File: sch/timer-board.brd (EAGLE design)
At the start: 76.2 x 69.9 mm, 35 parts, among them IC1 ATMEGA328P

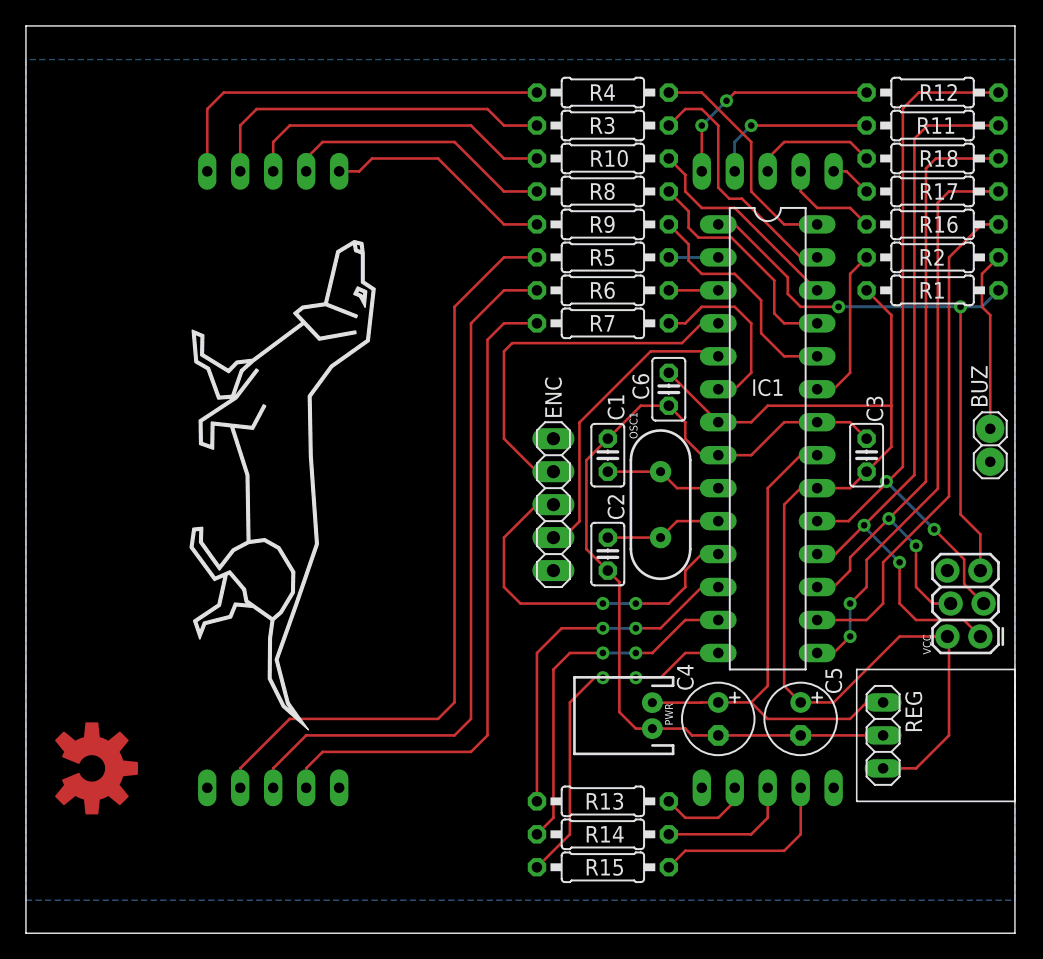
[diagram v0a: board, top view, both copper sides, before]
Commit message: feat: pcb added holes
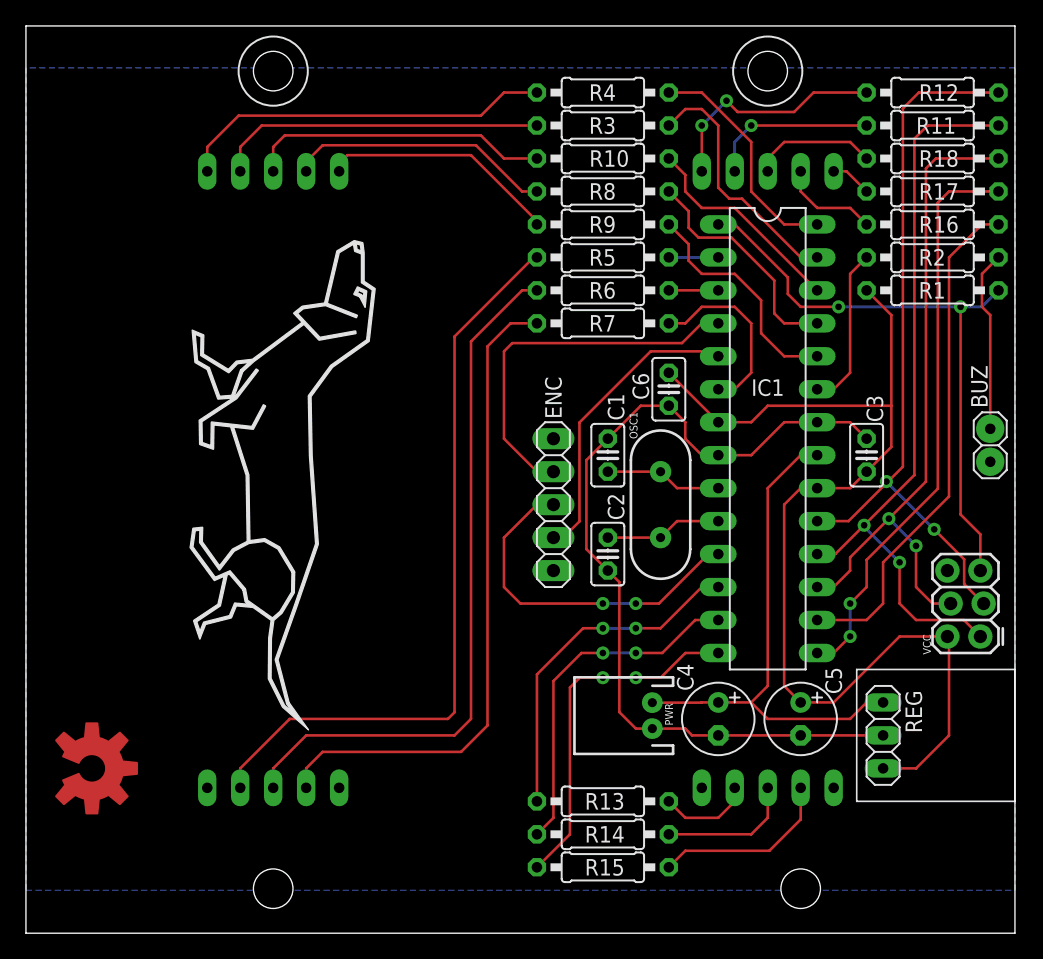
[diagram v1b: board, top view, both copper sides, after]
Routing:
- net N$1: track 27.4 -> 25.4 mm
- net N$2: track 30.7 -> 29.0 mm
- net D0C: track 27.5 -> 26.5 mm
- net N$3: track 58.5 -> 57.6 mm
- net N$9: track 24.2 -> 23.3 mm
- net N$4: track 54.9 -> 54.1 mm
- net BTN: track 28.0 -> 27.3 mm
- net N$5: track 51.3 -> 50.6 mm
- net N$7: track 17.8 -> 18.5 mm
- net N$14: track 17.3 -> 18.0 mm
- net D0E: track 26.8 -> 27.4 mm
- net N$17: track 14.8 -> 14.1 mm
- net D0D: track 27.5 -> 27.0 mm

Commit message: refactoring: reworked routing
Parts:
- removed C5: 100uF, rcl:E2,5-6
- removed REG: VREG_STEP_UP, parts:VREG
- added R19: (no value), rcl:0207/10
- added T1: 2N3904, transistor:TO92
- BUZ: value CONN_1X2 -> BUZZER2_IN_1; device parts:CONN_1X2 -> parts:BUZZER_2_IN_1
- C4: value 100uF -> 10uF
- LOGO1: value OSHW-LOGOL-COPPER -> OSHW-LOGOL; device SparkFun-Aesthetics:OSHW-LOGO-L_COPPER -> SparkFun-Aesthetics:OSHW-LOGO-L
- moved LOGO1 48.3 mm to (7.62, 61.0)
- moved R2 26.2 mm to (57.1, 29.2), turned to 90 degrees
- moved VCC 23.7 mm to (67.4, 45.7)
- moved BUZ 17.8 mm to (69.8, 19.1), turned to 180 degrees
- moved R1 13.0 mm to (57.1, 47.0), turned to 270 degrees
- moved R17 7.62 mm to (69.8, 64.8)
- moved PWR 5.88 mm to (42.5, 18.2), turned to 270 degrees
- moved R11 2.54 mm to (69.8, 59.7)
- moved R12 2.54 mm to (69.8, 62.2)
- moved R18 2.54 mm to (69.8, 57.1)
- moved C4 1.27 mm to (54.6, 16.5), turned to 90 degrees
- moved C6 0.90 mm to (50.2, 41.3)
- moved U$1 0.63 mm to (12.7, 54.0)
- moved C3 0.63 mm to (64.1, 36.8)
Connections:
- removed net VIN: C4.+, IC1.21, PWR.2, REG.3
- new net N$10: R2.1, T1.2
- net BTN: now also ENC.4; no longer ENC.3
- net BUZ: now also IC1.15; no longer IC1.23
- net D0C: now also IC1.14; no longer IC1.12
- net D0E: now also IC1.12; no longer IC1.14
- net D0G: now also IC1.23; no longer IC1.15
- net ENC1: now also ENC.3; no longer ENC.4
- net GND: now also BUZ.-, BUZ.-1, R19.1; no longer BUZ.2, C5.-, REG.2
- net N$8: now also BUZ.+, R19.2, T1.3; no longer BUZ.1, R2.1
- net VCC: now also C4.+, PWR.2, T1.1; no longer C5.+, REG.1
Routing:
- net VIN: track 40.7 -> 0.00 mm
- net RST: track 46.4 -> 22.1 mm, vias 2 -> 0
- net D0A: track 57.3 -> 42.3 mm
- net D0B: track 56.6 -> 42.1 mm
- net N$8: track 14.0 -> 28.0 mm
- net D0E: track 27.4 -> 38.7 mm, vias 2 -> 0
- net N$10: track 0.00 -> 11.1 mm
- net D0G: track 44.3 -> 33.6 mm, vias 2 -> 0
- net BTN: track 27.3 -> 16.8 mm, vias 2 -> 0
- net D0D: track 27.0 -> 35.1 mm, vias 2 -> 0
- net ENC2: track 29.0 -> 21.9 mm
- net D0P: track 51.7 -> 44.7 mm
- net D0C: track 26.5 -> 32.7 mm, vias 2 -> 0
- net N$19: track 3.18 -> 7.87 mm, vias 0 -> 1
- net N$5: track 50.6 -> 54.3 mm
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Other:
- board text added: "E1"
- board text added: "E2"
- board text added: "SW"
- board text added: "Timer board rev2"

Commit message: refactoring: finalized routing
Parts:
- removed C6: 1uF, rcl:C025-025X050
- removed IC1: ATMEGA328P, parts:DIL28
- removed VCC: (no value), SparkFun-Connectors:2X3_LOCK
- added C5: 10uF, rcl:E2,5-6
- added J1: (no value), SparkFun-Connectors:1X02_LOCK
- added PROG: (no value), SparkFun-Connectors:2X3_LOCK
- added R20: (no value), rcl:RTRIM3296W
- added U2: 328P, SparkFun-IC-Microcontroller:DIP28
- BUZ: value BUZZER2_IN_1 -> CONN_1X2JST; device parts:BUZZER_2_IN_1 -> parts:1X02_LOCK_JST
- C1, C2: device rcl:C025-025X050 -> rcl:C050-024X044
- C3: value 1uF -> 0.1uF; device rcl:C025-025X050 -> rcl:C050-024X044
- C4: value 10uF -> 0.1uF; device rcl:E2,5-6 -> rcl:C050-024X044
- DIGIT0, DIGIT1: value 7-SEGMENT-DISPLAY -> 7_SEGMENT_DISPLAY; device parts:1.8-INCH -> parts:7_SEGMENT_1.8_INCH
- ENC: value CONN_1X5CONN_1X5 -> CONN_1X5; device parts:CONN_1X5 -> parts:1X05_LOCK_JST
- PWR: value (none) -> 5V; device SparkFun-Connectors:JST-2-PTH -> parts:1X02_LOCK_JST
- R10: value 10k -> (none)
- R9: value 3k -> (none)
- moved C4 26.5 mm to (47.0, 41.9), turned to 180 degrees
- moved R19 25.5 mm to (69.8, 10.2), turned to 180 degrees
- moved BUZ 14.0 mm to (68.6, 5.08), turned to 0 degrees
- moved R9 7.62 mm to (44.5, 47.0)
- moved PWR 4.67 mm to (39.4, 21.6)
- moved ENC 4.02 mm to (39.4, 39.4)
- moved R14 2.54 mm to (44.5, 10.2)
- moved R10 2.54 mm to (44.5, 57.1)
- moved R11 2.54 mm to (69.8, 57.1)
- moved R12 2.54 mm to (69.8, 59.7)
- moved R13 2.54 mm to (44.5, 12.7)
- moved R16 2.54 mm to (69.8, 52.1)
- moved R18 2.54 mm to (69.8, 54.6)
- moved R3 2.54 mm to (44.5, 59.7)
- moved R7 2.54 mm to (44.5, 44.5)
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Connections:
- removed net N$8: BUZ.+, R19.2, T1.3
- new net N$11: C5.+, J1.2, PWR.2
- new net N$12: R20.1, T1.3
- new net N$21: BUZ.2, R19.2, R20.2
- net BTN: now also U2.11; no longer IC1.11
- net BUZ: now also U2.15; no longer IC1.15
- net D0A: now also PROG.1, U2.18; no longer IC1.18, VCC.1
- net D0B: now also PROG.3, U2.19; no longer IC1.19, VCC.3
- net D0C: now also U2.14; no longer IC1.14
- net D0D: now also U2.13; no longer IC1.13
- net D0E: now also U2.12; no longer IC1.12
- net D0F: now also U2.16; no longer IC1.16
- net D0G: now also U2.23; no longer IC1.23
- net D0P: now also PROG.4, U2.17; no longer IC1.17, VCC.4
- net D1A: now also U2.27; no longer IC1.27
- net D1B: now also U2.28; no longer IC1.28
- net D1C: now also U2.2; no longer IC1.2
- net D1D: now also U2.3; no longer IC1.3
- net D1E: now also U2.6; no longer IC1.6
- net D1F: now also U2.25; no longer IC1.25
- net D1G: now also U2.24; no longer IC1.24
- net D1P: now also U2.26; no longer IC1.26
- net ENC1: now also U2.5; no longer IC1.5
- net ENC2: now also U2.4; no longer IC1.4
- net GND: now also BUZ.1, C4.2, C5.-, PROG.6, U2.22, U2.8; no longer BUZ.-, BUZ.-1, C4.-, C6.2, IC1.22, IC1.8, VCC.6
- net RST: now also PROG.5, U2.1; no longer IC1.1, VCC.5
- net VCC: now also C4.1, J1.1, PROG.2, U2.20, U2.7; no longer C4.+, C6.1, IC1.20, IC1.7, PWR.2, VCC.2
- net XTAL1: now also U2.9; no longer IC1.9
- net XTAL2: now also U2.10; no longer IC1.10
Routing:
- net N$8: track 28.0 -> 0.00 mm
- net N$21: track 0.00 -> 28.0 mm
- net N$11: track 0.00 -> 17.8 mm
- net N$7: track 20.3 -> 34.8 mm
- net N$12: track 0.00 -> 11.7 mm
- net VCC: track 84.7 -> 73.1 mm, vias 0 -> 1
- net D1E: track 13.8 -> 5.61 mm
- net N$19: track 7.87 -> 15.2 mm, vias 1 -> 0
- net N$6: track 21.6 -> 27.6 mm
- net BTN: track 16.8 -> 22.5 mm
- net N$9: track 23.3 -> 28.5 mm
- net N$5: track 54.3 -> 49.4 mm
- net N$13: track 12.1 -> 16.9 mm
- net D1G: track 19.6 -> 15.0 mm
- net GND: track 68.5 -> 72.9 mm
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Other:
- outline, holes or cut-outs redrawn
- board text added: "+"
- board text added: "GND"
- board text added: "Timer Board Rev.2 Mathieu Brun - 2019"
- board text added: "VCC"
- board text removed: "Timer board rev2"

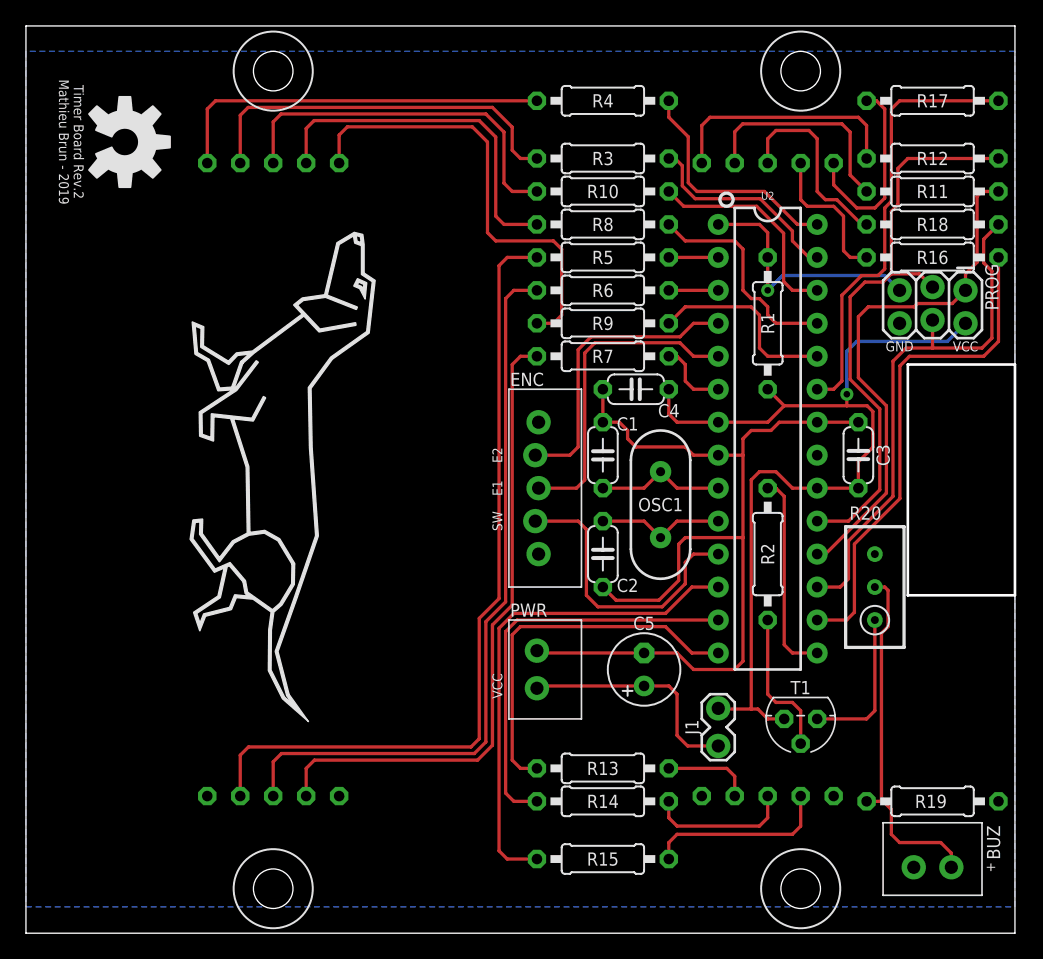
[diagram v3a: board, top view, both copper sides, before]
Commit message: refactoring: added vcc pour, updated capacitors footprints fix: correct orientation of 7segment displays
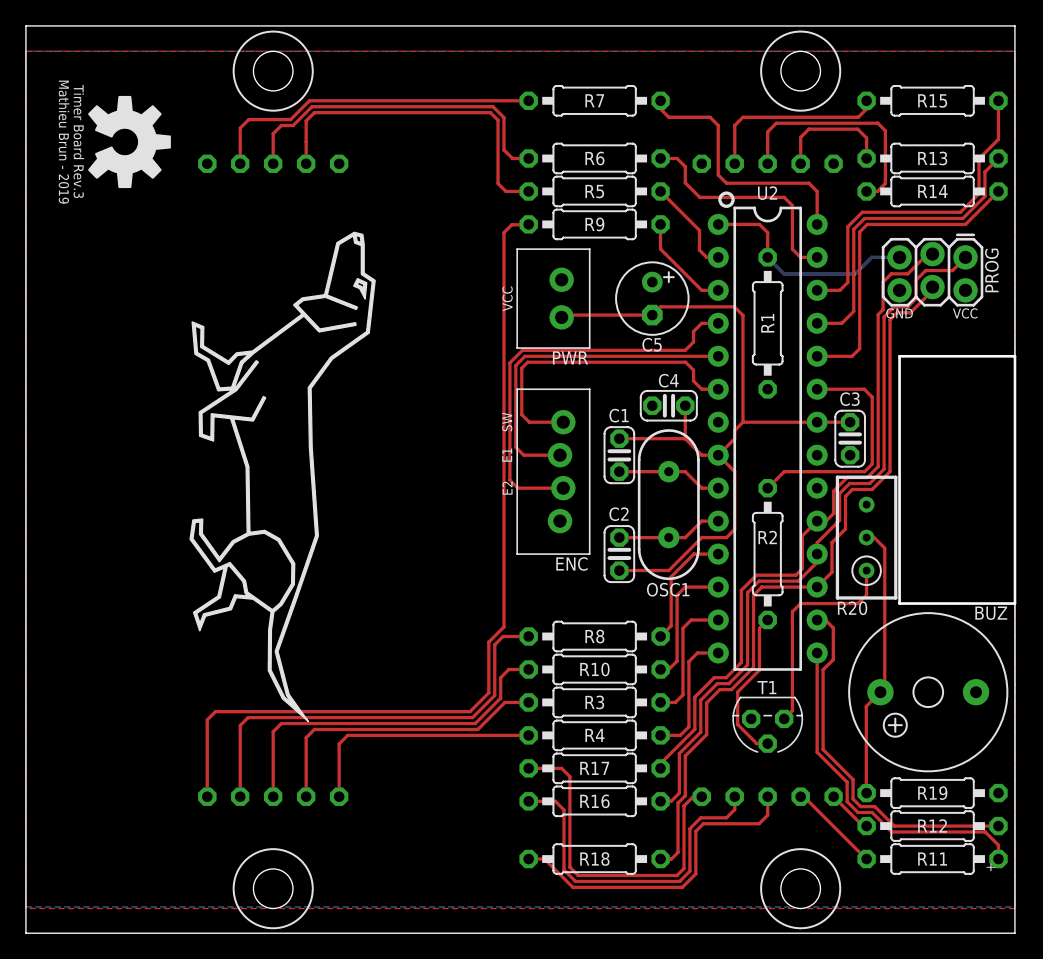
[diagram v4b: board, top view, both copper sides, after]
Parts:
- removed J1: (no value), SparkFun-Connectors:1X02_LOCK
- BUZ: value CONN_1X2JST -> BUZZER; device parts:1X02_LOCK_JST -> parts:BUZZER
- C1, C2, C3, C4: device rcl:C050-024X044 -> rcl:C025-024X044
- ENC: device parts:1X05_LOCK_JST -> parts:1X04_LOCK_JST
- moved R15 63.7 mm to (69.8, 64.1), turned to 180 degrees
- moved R17 57.6 mm to (43.8, 12.7)
- moved R18 55.4 mm to (43.8, 5.71)
- moved R13 53.4 mm to (69.8, 59.7), turned to 180 degrees
- moved R14 53.4 mm to (69.8, 57.1), turned to 180 degrees
- moved R11 51.4 mm to (69.8, 5.71)
- moved R12 51.4 mm to (69.8, 8.26)
- moved R16 49.3 mm to (43.8, 10.2)
- moved R4 48.9 mm to (43.8, 15.2)
- moved R3 41.9 mm to (43.8, 17.8)
- moved DIGIT0 38.1 mm to (19.1, 34.9), turned to 180 degrees
- moved DIGIT1 38.1 mm to (57.1, 34.9), turned to 180 degrees
- moved R10 36.8 mm to (43.8, 20.3)
- moved R8 31.8 mm to (43.8, 22.9)
- moved C5 28.6 mm to (48.3, 48.9), turned to 270 degrees
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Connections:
- removed net N$11: C5.+, J1.2, PWR.2
- net BTN: now also U2.6; no longer U2.11
- net BUZ: now also U2.23; no longer U2.15
- net D0A: now also U2.15; no longer PROG.1, U2.18
- net D0B: now also U2.16; no longer PROG.3, U2.19
- net D0C: now also U2.25; no longer U2.14
- net D0D: now also U2.24; no longer U2.13
- net D0E: now also U2.26; no longer U2.12
- net D0F: now also PROG.1, U2.18; no longer U2.16
- net D0G: now also PROG.3, U2.19; no longer U2.23
- net D1A: now also U2.13; no longer U2.27
- net D1B: now also U2.14; no longer U2.28
- net D1D: now also U2.27; no longer U2.3
- net D1E: now also U2.28; no longer U2.6
- net D1F: now also U2.11; no longer U2.25
- net D1G: now also U2.3; no longer U2.24
- net D1P: now also U2.12; no longer U2.26
- net GND: now also BUZ.-; no longer BUZ.1, ENC.5
- net N$1: now also DIGIT0.9; no longer DIGIT1.9
- net N$13: now also DIGIT1.9; no longer DIGIT0.9
- net N$14: now also DIGIT1.10; no longer DIGIT0.10
- net N$15: now also DIGIT1.4; no longer DIGIT0.4
- net N$16: now also DIGIT1.3; no longer DIGIT0.3
- net N$17: now also DIGIT1.2; no longer DIGIT0.2
- net N$18: now also DIGIT1.7; no longer DIGIT0.7
- net N$19: now also DIGIT1.6; no longer DIGIT0.6
- net N$2: now also DIGIT0.10; no longer DIGIT1.10
- net N$20: now also DIGIT1.8; no longer DIGIT0.8
- net N$21: now also BUZ.+; no longer BUZ.2
- net N$3: now also DIGIT0.4; no longer DIGIT1.4
- net N$4: now also DIGIT0.3; no longer DIGIT1.3
- net N$5: now also DIGIT0.2; no longer DIGIT1.2
- net N$6: now also DIGIT0.7; no longer DIGIT1.7
- net N$7: now also DIGIT0.6; no longer DIGIT1.6
- net N$9: now also DIGIT0.8; no longer DIGIT1.8
- net VCC: now also C5.+, PWR.2; no longer J1.1
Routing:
- net VCC: track 73.1 -> 0.00 mm, vias 1 -> 0
- net N$3: track 62.4 -> 26.1 mm
- net N$7: track 34.8 -> 66.6 mm
- net N$4: track 57.1 -> 26.0 mm
- net N$5: track 49.4 -> 25.8 mm
- net D0G: track 34.0 -> 52.9 mm
- net D0F: track 38.4 -> 57.1 mm
- net N$11: track 17.8 -> 0.00 mm
- net D0B: track 45.5 -> 28.0 mm
- net D0P: track 40.9 -> 57.8 mm
- net N$14: track 18.7 -> 3.48 mm
- net N$18: track 11.3 -> 26.3 mm
- net D1E: track 5.61 -> 20.1 mm
- net D1D: track 3.81 -> 17.9 mm
- net D0A: track 40.3 -> 26.5 mm
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- added copper zone on layer 1, net VCC
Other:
- outline, holes or cut-outs redrawn
- board text added: "Timer Board Rev.3 Mathieu Brun - 2019"
- board text removed: "Timer Board Rev.2 Mathieu Brun - 2019"

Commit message: fix: clearance around milling, moved resistors, removed buzzer resistor
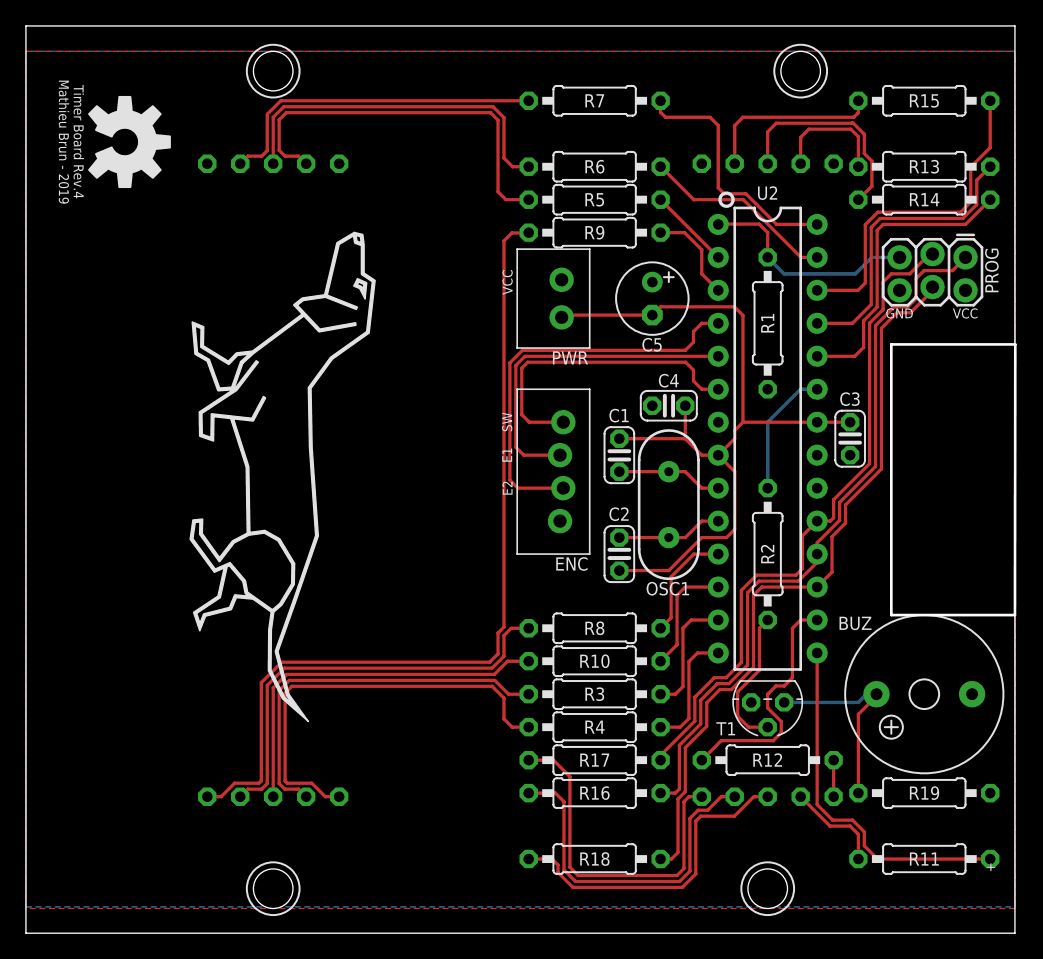
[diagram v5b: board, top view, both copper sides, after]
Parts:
- removed R20: (no value), rcl:RTRIM3296W
- moved R12 13.7 mm to (57.1, 13.3), turned to 0 degrees
- moved T1 1.27 mm to (57.1, 17.8)
- moved R13 0.90 mm to (69.2, 59.1)
- moved R14 0.90 mm to (69.2, 56.5)
- moved R17 0.64 mm to (43.8, 13.3)
- moved R8 0.64 mm to (43.8, 23.5)
- moved R16 0.63 mm to (43.8, 10.8)
- moved R4 0.63 mm to (43.8, 15.9)
- moved R10 0.63 mm to (43.8, 21.0)
- moved R3 0.63 mm to (43.8, 18.4)
- moved R5 0.63 mm to (43.8, 56.5)
- moved R6 0.63 mm to (43.8, 59.1)
- moved R9 0.63 mm to (43.8, 54.0)
- moved R11 0.63 mm to (69.2, 5.71)
- moved R15 0.63 mm to (69.2, 64.1)
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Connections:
- removed net N$12: R20.1, T1.3
- net N$21: now also T1.3; no longer R20.2
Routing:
- net N$12: track 16.6 -> 0.00 mm
- net N$2: track 18.9 -> 32.7 mm
- net D0B: track 28.0 -> 18.8 mm
- net BUZ: track 18.5 -> 9.94 mm
- net N$1: track 22.8 -> 29.7 mm
- net N$21: track 21.2 -> 15.6 mm
- net N$3: track 26.1 -> 30.3 mm
- net D1D: track 17.9 -> 15.0 mm
- net N$16: track 17.8 -> 16.2 mm
- net D0D: track 24.5 -> 23.0 mm
- net N$4: track 26.0 -> 27.3 mm
- net D0G: track 52.9 -> 51.5 mm
- net N$9: track 27.6 -> 28.9 mm
- net D0F: track 57.1 -> 55.9 mm
- net D1C: track 7.44 -> 6.29 mm
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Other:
- outline, holes or cut-outs redrawn
- board text added: "Timer Board Rev.4 Mathieu Brun - 2019"
- board text removed: "Timer Board Rev.3 Mathieu Brun - 2019"
